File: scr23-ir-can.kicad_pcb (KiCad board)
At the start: 2 copper layers, 17 parts, among them J1 22-24AWG, J2 22-24AWG, J3 22-24AWG, J4 22-24AWG, U2 AP63205WU, U4 ADM3051CRZ, U5 STM32L431KBUx, U6 AP2127K-3.3

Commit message: schematic done, added stdc14 programming connector
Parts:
- added C10: 10uF, Capacitor_SMD:C_0603_1608Metric_Pad1.08x0.95mm_HandSolder, F.Cu at (103.8, 106.4)
- U1: value ~ -> Sparkfun MLX90640 Breakout
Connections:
- U5 pad 1: unconnected-(U5-VDD-Pad1) -> +3.3V
- U5 pad 16: Net-(U5-VSS-Pad16) -> GND
- U5 pad 17: unconnected-(U5-VDD-Pad17) -> +3.3V
- U5 pad 19: unconnected-(U5-PA9-Pad19) -> /IR_SCL
- U5 pad 20: unconnected-(U5-PA10-Pad20) -> /IR_SDA
- U5 pad 31: unconnected-(U5-PH3-Pad31) -> Net-(U5-PH3)
- U5 pad 32: Net-(U5-VSS-Pad16) -> GND
- U5 pad 33: Net-(U5-VSS-Pad16) -> GND
- U5 pad 5: unconnected-(U5-VDDA-Pad5) -> +3.3V

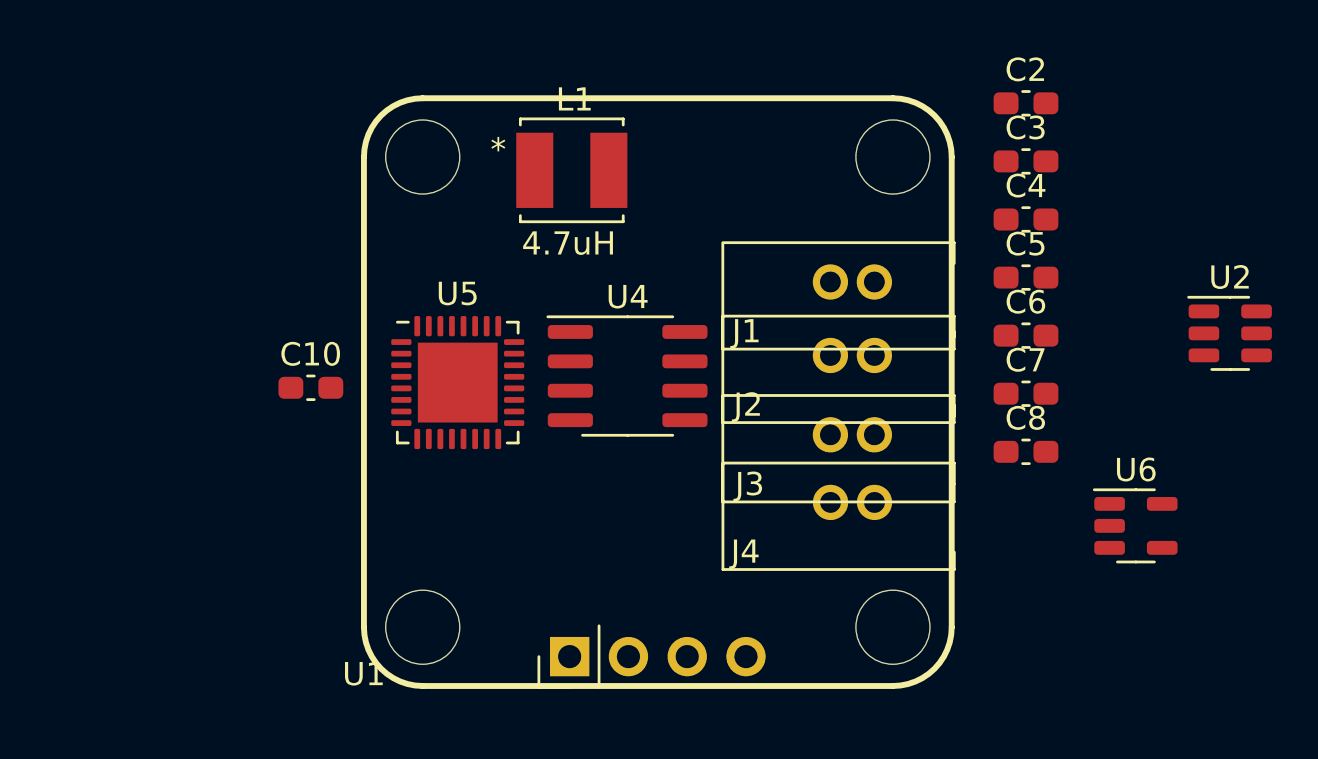
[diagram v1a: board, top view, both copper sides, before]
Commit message: add edge cuts
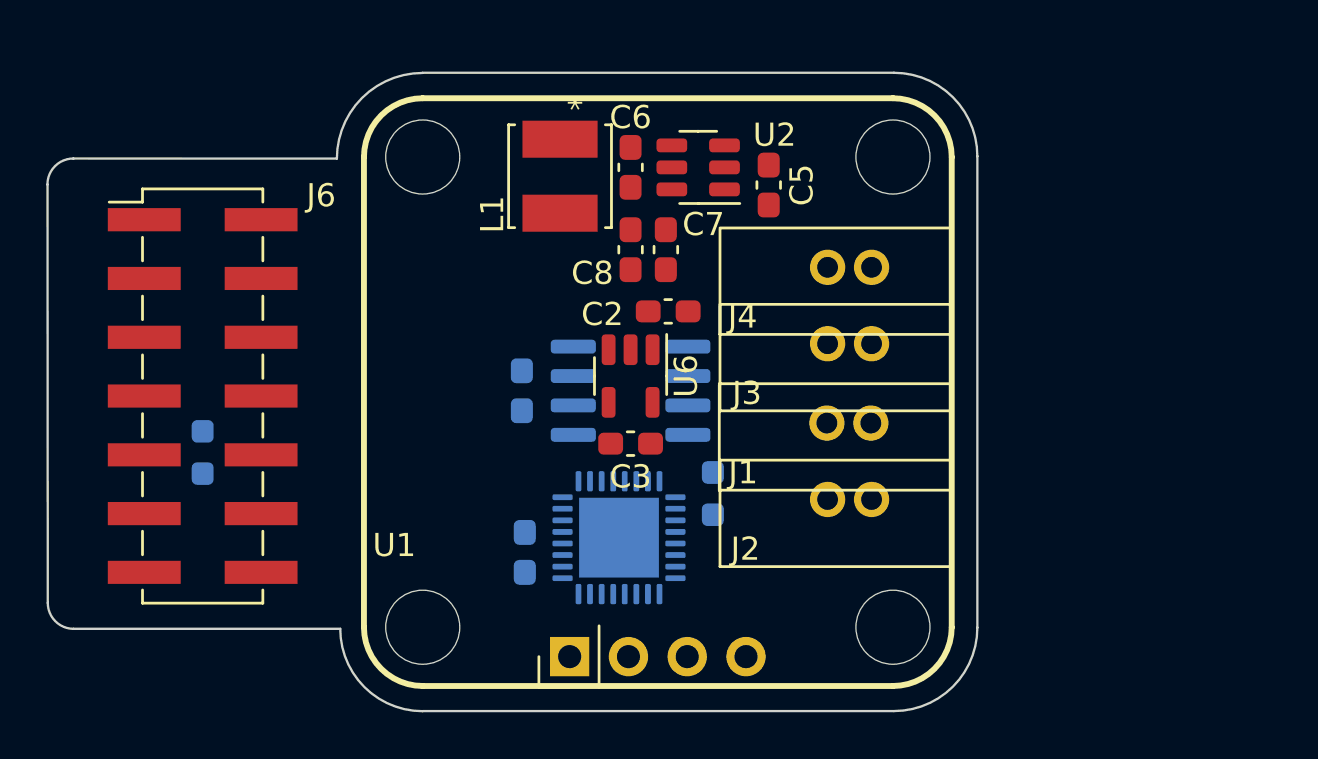
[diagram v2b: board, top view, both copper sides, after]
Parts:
- added J6: Conn_ST_STDC14, Connector_PinHeader_2.54mm:PinHeader_2x07_P2.54mm_Vertical_SMD, F.Cu at (99.1, 106.8)
- added R1: 100, Resistor_SMD:R_0603_1608Metric_Pad0.98x0.95mm_HandSolder, B.Cu at (99.1, 109.2)
- added R2: 10k, Resistor_SMD:R_0603_1608Metric_Pad0.98x0.95mm_HandSolder, B.Cu at (121.2, 111.0)
- C10, C4, U4, U5: moved to B.Cu
- moved U2 24.1 mm to (120.5, 96.9), turned to 180 degrees
- moved C4 23.0 mm to (112.9, 106.6), turned to -90 degrees
- moved U6 22.8 mm to (117.6, 105.9), turned to -90 degrees
- moved C3 21.0 mm to (117.6, 108.8), turned to 180 degrees
- moved C8 19.2 mm to (117.6, 100.5), turned to 90 degrees
- moved C6 18.6 mm to (117.6, 96.9), turned to -90 degrees
- moved C2 17.9 mm to (119.2, 103.1), turned to 180 degrees
- moved C7 16.8 mm to (119.1, 100.5), turned to -90 degrees
- moved C5 11.8 mm to (123.6, 97.7), turned to -90 degrees
- moved C10 11.7 mm to (113.0, 113.5), turned to 90 degrees
- moved J4 10.2 mm to (126.1, 101.2)
- moved U5 9.67 mm to (117.1, 112.9), turned to 180 degrees
- moved J2 6.22 mm to (126.1, 111.3)
- moved J1 6.10 mm to (126.1, 108.0)
- moved J3 3.94 mm to (126.1, 104.5)
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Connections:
- U5 pad 23: unconnected-(U5-PA13-Pad23) -> /SWDIO
- U5 pad 24: unconnected-(U5-PA14-Pad24) -> /SWCLK
- U5 pad 26: unconnected-(U5-PB3-Pad26) -> /SWO
- U5 pad 4: unconnected-(U5-NRST-Pad4) -> /nRST
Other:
- board outline added: 40.2 x 27.6 mm

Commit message: added comment for maybe replacing the STDC14 thing
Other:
- board text added: "NOTE: Let's maybe make the debug connector disconnectable somehow? Maybe break off board to board connector, or I could make a little adapter that goes to a JST connector or something that could be on that side of the board much more compactly?"
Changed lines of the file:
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@@
   (gr_line (start 93.5228 116.839999) (end 105.055846 116.839999)
     (stroke (width 0.1) (type default)) (layer "Edge.Cuts"))
+  (gr_text "NOTE: Let's maybe make the debug connector disconnectable somehow? Maybe\nbreak off board to board connector, or I could make a little adapter that\ngoes to a JST connector or something that could be on that side of the board\nmuch more compactly?" (at 79.5528 92.0496) (layer "User.1")
+    (effects (font (size 1 1) (thickness 0.15)) (justify left bottom))
+  )
 )

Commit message: change to a through hole 2x7 for programming
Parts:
- J6: footprint Connector_PinHeader_2.54mm:PinHeader_2x07_P2.54mm_Vertical_SMD -> Connector_PinHeader_2.54mm:PinHeader_2x07_P2.54mm_Vertical
- moved J6 7.75 mm to (99.7, 99.1)
- moved R1 5.80 mm to (104.9, 109.0)
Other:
- board size 40.2 x 27.6 mm -> 35.3 x 27.6 mm
- board text added: "NOTE: Let's maybe make the debug connector disconnectable somehow? Maybe break off board to board connector, or I could make a little adapter that goes to a JST connector or something that could be on that side of the board much more compactly? Maybe even bigger IQ: expose some of the I/O of this board with a small JST connector or something so we can expand what sensors this guy hosts later?"
- board text removed: "NOTE: Let's maybe make the debug connector disconnectable somehow? Maybe break off board to board connector, or I could make a little adapter that goes to a JST connector or something that could be on that side of the board much more compactly?"

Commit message: misc changes to layout, need to move everything to same layer
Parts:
- moved R2 0.14 mm to (121.0, 110.9)
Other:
- outline, holes or cut-outs redrawn
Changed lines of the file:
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@@
   )
   (footprint "Resistor_SMD:R_0603_1608Metric_Pad0.98x0.95mm_HandSolder" (layer "B.Cu")
-    (at 121.158 110.998 -90)
+    (at 121.031 110.9472 -90)
     (descr "Resistor SMD 0603 (1608 Metric), square (rectangular) end terminal, IPC_7351 nominal with elongated pad for handsoldering. (Body size source: IPC-SM-782 page 72, https://www.pcb-3d.com/wordpress/wp-content/uploads/ipc-sm-782a_amendment_1_and_2.pdf), generated with kicad-footprint-generator")
     (tags "resistor handsolder")
@@
     (property "ki_keywords" "R res resistor")
     (attr smd)
-    (fp_text reference "R2" (at 0 1.43 90) (layer "B.SilkS")
+    (fp_text reference "R2" (at 2.5146 -0.1778 90) (layer "B.SilkS")
         (effects (font (size 1 1) (thickness 0.15)) (justify mirror))
     )
@@
     )
   )
-  (gr_arc (start 97.273206 97.637599) (mid 97.601393 96.845286) (end 98.393706 96.517099)
+  (gr_arc (start 97.334813 97.637599) (mid 97.663 96.845286) (end 98.455313 96.517099)
     (stroke (width 0.1) (type default)) (layer "Edge.Cuts"))
   (gr_arc (start 108.616435 120.400588) (mid 106.098718 119.357716) (end 105.055846 116.839999)
     (stroke (width 0.1) (type default)) (layer "Edge.Cuts"))
-  (gr_line (start 97.276106 97.637599) (end 97.287893 115.722401)
+  (gr_line (start 97.337713 97.637599) (end 97.3495 115.722401)
     (stroke (width 0.1) (type default)) (layer "Edge.Cuts"))
   (gr_arc (start 132.588 116.7892) (mid 131.531593 119.339593) (end 128.9812 120.396)
@@
   (gr_arc (start 128.981199 92.811601) (mid 131.531592 93.868008) (end 132.587999 96.418401)
     (stroke (width 0.1) (type default)) (layer "Edge.Cuts"))
-  (gr_line (start 98.298 96.52) (end 104.910361 96.52)
+  (gr_line (start 98.4504 96.52) (end 104.910361 96.52)
     (stroke (width 0.1) (type default)) (layer "Edge.Cuts"))
   (gr_arc (start 104.910361 96.52) (mid 105.994077 93.903677) (end 108.6104 92.819961)
@@
   (gr_line (start 108.6104 92.811601) (end 128.981199 92.811601)
     (stroke (width 0.1) (type default)) (layer "Edge.Cuts"))
-  (gr_arc (start 98.408393 116.842901) (mid 97.616088 116.51471) (end 97.287893 115.722401)
+  (gr_arc (start 98.47 116.842901) (mid 97.677695 116.51471) (end 97.3495 115.722401)
     (stroke (width 0.1) (type default)) (layer "Edge.Cuts"))
   (gr_line (start 132.587999 96.418401) (end 132.588 116.7892)
     (stroke (width 0.1) (type default)) (layer "Edge.Cuts"))
-  (gr_line (start 98.298 116.839999) (end 105.055846 116.839999)
+  (gr_line (start 98.4504 116.839999) (end 105.055846 116.839999)
     (stroke (width 0.1) (type default)) (layer "Edge.Cuts"))
   (gr_text "NOTE: Let's maybe make the debug connector disconnectable somehow? Maybe\nbreak off board to board connector, or I could make a little adapter that\ngoes to a JST connector or something that could be on that side of the board\nmuch more compactly?\n\nMaybe even bigger IQ: expose some of the I/O of this board with a small JST\nconnector or something so we can expand what sensors this guy hosts later?" (at 86.868 134.62) (layer "User.1")

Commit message: better layout lol
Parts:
- C10, C4, R1, R2, U4, U5: moved to F.Cu
- moved C2 10.0 mm to (109.2, 103.7), turned to 0 degrees
- moved C3 8.48 mm to (109.2, 109.8)
- moved U6 8.45 mm to (109.2, 106.7)
- moved J1 1.09 mm to (127.2, 108.0)
- moved J2 1.09 mm to (127.2, 111.3)
- moved J3 1.09 mm to (127.2, 104.5)
- moved J4 1.09 mm to (127.2, 101.2)
- turned U4 to 180 degrees
- turned U5 to 0 degrees

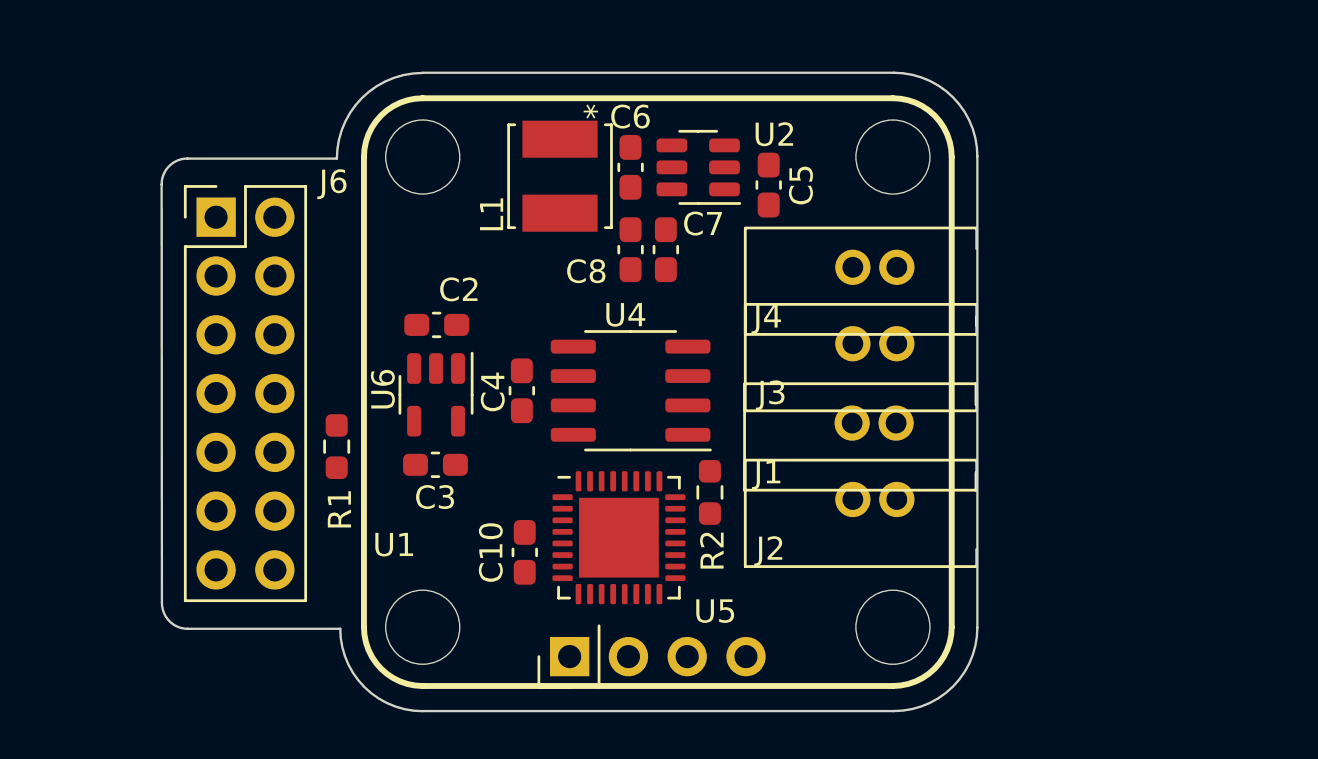
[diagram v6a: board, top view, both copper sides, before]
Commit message: change programming boi to 1.27mm instead of 2.54, i had it wrong
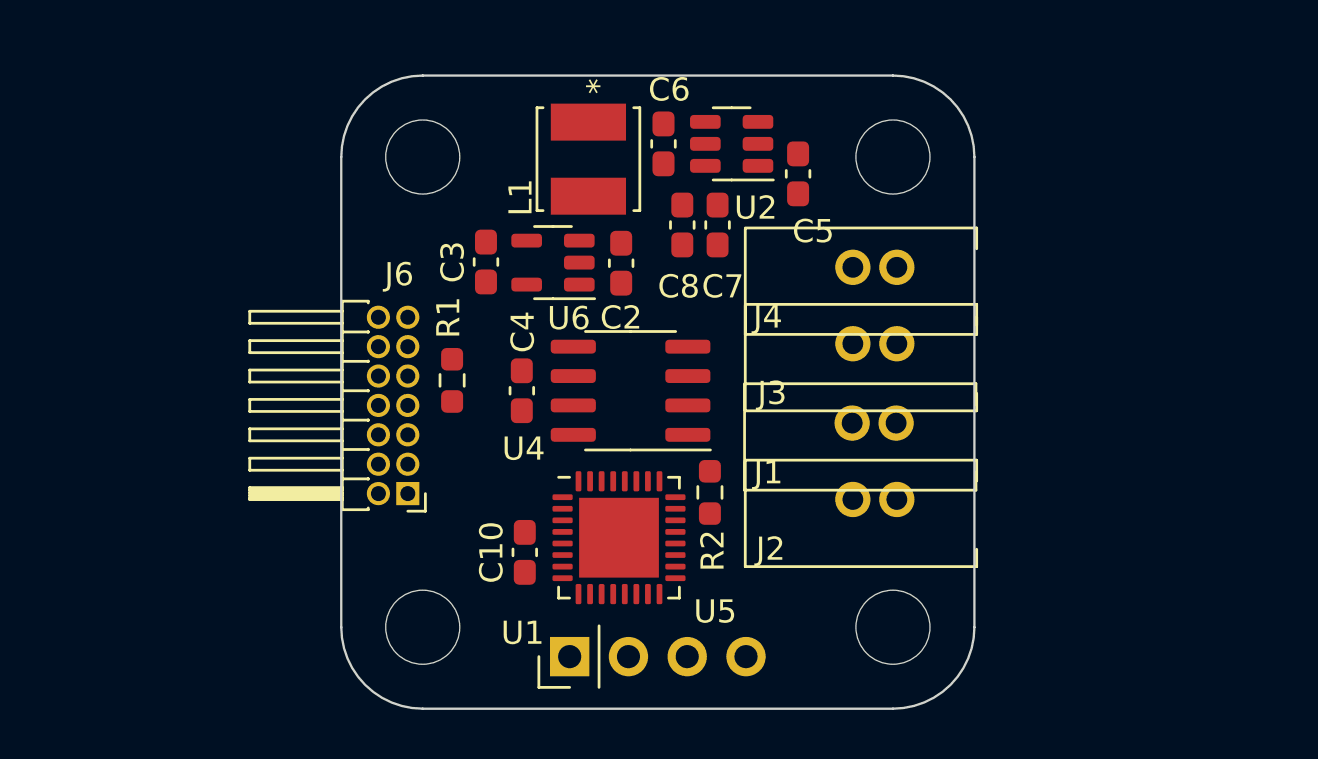
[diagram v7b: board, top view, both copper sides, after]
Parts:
- J6: footprint Connector_PinHeader_2.54mm:PinHeader_2x07_P2.54mm_Vertical -> Connector_PinHeader_1.27mm:PinHeader_2x07_P1.27mm_Horizontal
- moved J6 14.5 mm to (108.0, 111.0), turned to 180 degrees
- moved C3 9.03 mm to (111.4, 101.0), turned to 90 degrees
- moved C2 8.41 mm to (117.2, 101.0), turned to -90 degrees
- moved U6 7.63 mm to (114.2, 101.0), turned to 180 degrees
- moved R1 5.75 mm to (109.9, 106.1), turned to -90 degrees
- moved C7 2.48 mm to (121.4, 99.4)
- moved C8 2.48 mm to (119.8, 99.4)
- moved U2 1.77 mm to (122.0, 95.9)
- moved C6 1.75 mm to (119.0, 95.9)
- moved L1 1.43 mm to (115.8, 96.5)
- moved C5 1.36 mm to (124.8, 97.2)
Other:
- board size 35.3 x 27.6 mm -> 27.4 x 27.4 mm
- board text removed: "NOTE: Let's maybe make the debug connector disconnectable somehow? Maybe break off board to board connector, or I could make a little adapter that goes to a JST connector or something that could be on that side of the board much more compactly? Maybe even bigger IQ: expose some of the I/O of this board with a small JST connector or something so we can expand what sensors this guy hosts later?"

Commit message: pcb finished
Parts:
- added C9: 10uF, Capacitor_SMD:C_0603_1608Metric_Pad1.08x0.95mm_HandSolder, F.Cu at (121.2, 111.0)
- moved R2 8.20 mm to (113.2, 113.3)
- moved C10 6.23 mm to (118.6, 116.3), turned to 0 degrees
- moved R1 4.87 mm to (108.2, 101.5), turned to 180 degrees
- moved J6 1.04 mm to (109.0, 111.2)
- moved U5 0.48 mm to (117.1, 112.4), turned to 90 degrees
- turned U4 to 0 degrees
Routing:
- net GND: track 0.00 -> 25.0 mm, vias 0 -> 22
- net /nRST: track 0.00 -> 21.3 mm, vias 0 -> 2
- net /IR_SCL: track 0.00 -> 18.2 mm, vias 0 -> 2
- net /IR_SDA: track 0.00 -> 17.5 mm, vias 0 -> 3
- net /SWCLK: track 0.00 -> 15.1 mm, vias 0 -> 2
- net /SWO: track 0.00 -> 14.9 mm, vias 0 -> 2
- net /SWDIO: track 0.00 -> 14.2 mm, vias 0 -> 2
- net /CANH: track 0.00 -> 11.9 mm
- net /CANL: track 0.00 -> 11.5 mm
- net +12V: track 0.00 -> 10.6 mm
- net /CAN_TX: track 0.00 -> 7.73 mm, vias 0 -> 2
- net Net-(U2-SW): track 0.00 -> 5.44 mm
- net /CAN_RX: track 0.00 -> 4.79 mm, vias 0 -> 2
- net Net-(J6-GNDDetect): track 0.00 -> 3.91 mm
- net +3.3V: track 0.00 -> 3.39 mm
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- added copper zone on F.Cu, net +3.3V
- added copper zone on F.Cu, net +5V
- added copper zone on B.Cu, net GND
